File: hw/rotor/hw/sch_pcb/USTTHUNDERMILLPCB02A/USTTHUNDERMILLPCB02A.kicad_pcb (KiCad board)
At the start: 2 copper layers, 80 x 80 mm, 1 part, among them J1 HEADER_1x01

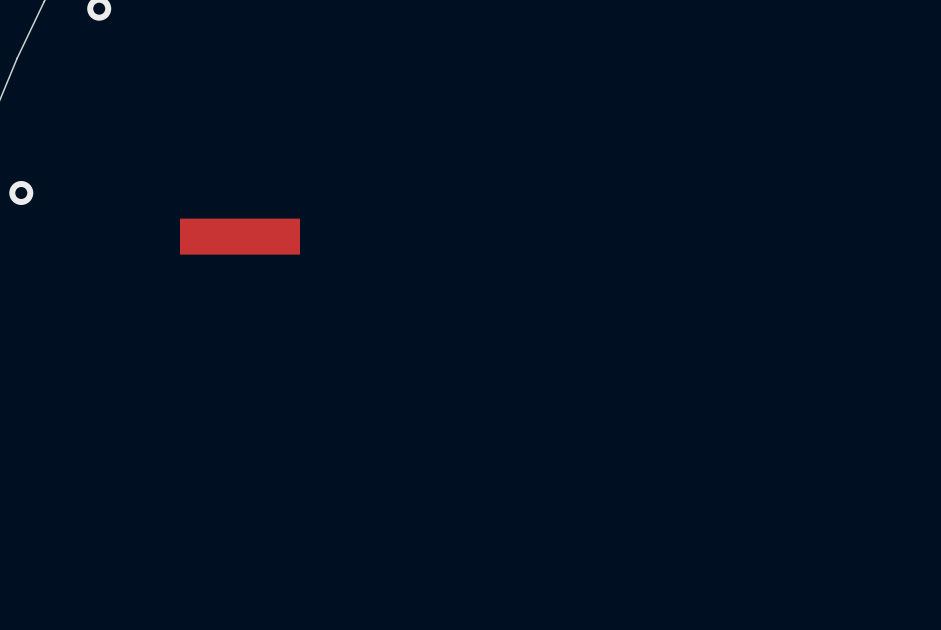
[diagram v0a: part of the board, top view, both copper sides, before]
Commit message: Add dimensions to PCB and improve readme.
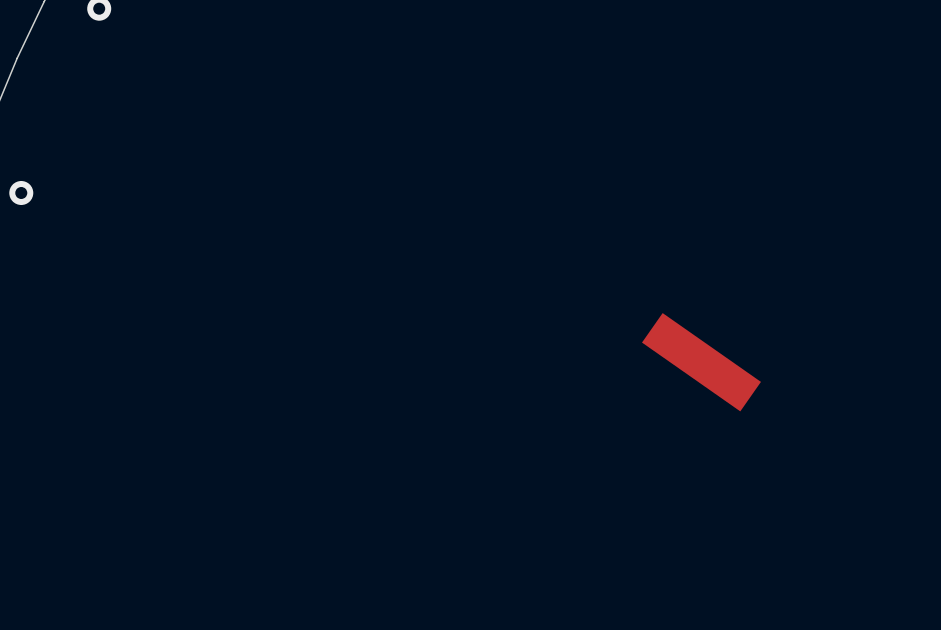
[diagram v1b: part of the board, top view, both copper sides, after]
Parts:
- moved J1 15.9 mm to (126.3, 83.9), turned to -35 degrees
